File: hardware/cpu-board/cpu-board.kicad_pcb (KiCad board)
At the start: 2 copper layers, 149.4 x 89.9 mm, 39 parts, among them P1 DATA, P2 ADDR1, P3 ADDR2, P4 CTRL1, P5 CTRL2, P6 PWR, P7 IO, SW1 RESET, U1 WD65C02, U2 AT28C256, U3 MXO45HS, U4 74HC132, U5 CY7C199, U6 4012, U7 4012, U8 74HC138, U9 7805

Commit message: layout
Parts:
- moved D1 125.7 mm to (254.0, 57.1)
- moved D2 125.7 mm to (188.0, 54.6)
- moved R6 125.7 mm to (257.8, 57.1)
- moved U9 125.7 mm to (205.7, 55.9)
- moved C12 125.7 mm to (196.8, 55.9)
- moved C7 125.7 mm to (217.2, 55.9)
- moved P6 125.7 mm to (175.3, 59.7)
- moved R7 125.7 mm to (250.2, 57.1)
- moved SW1 125.7 mm to (242.6, 57.1)
- moved C11 125.7 mm to (262.9, 59.7)
- moved C8 125.7 mm to (262.9, 53.3)
- moved R5 125.7 mm to (231.1, 54.6)
- moved C9 83.5 mm to (52.1, 74.9), turned to 180 degrees
- moved U4 62.5 mm to (72.4, 124.5), turned to 270 degrees
- moved P5 55.0 mm to (130.8, 55.9)
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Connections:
- P4 pad 1: +5V -> /VIN
- P4 pad 3: /VIN -> RDY
- P4 pad 4: SYNC -> ~IRQ
- P4 pad 5: ~IRQ -> +5V
- P4 pad 6: RDY -> SYNC
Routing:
- net GND: track 0.00 -> 405.8 mm, vias 0 -> 9
- net PHI2: track 62.5 -> 161.1 mm
- net BE: track 16.5 -> 72.9 mm
- net A14: track 176.0 -> 136.7 mm, vias 6 -> 7
- net A4: track 87.0 -> 125.8 mm, vias 0 -> 4
- net A7: track 87.0 -> 125.1 mm, vias 0 -> 2
- net A8: track 137.3 -> 102.4 mm, vias 6 -> 5
- net A12: track 121.8 -> 87.7 mm
- net Net-(U6-Pad1): track 33.3 -> 0.00 mm
- net /VIN: track 33.3 -> 0.00 mm
- net /~RAMCE: track 39.9 -> 71.6 mm
- net A13: track 121.0 -> 93.5 mm, vias 2 -> 5
- net Net-(R5-Pad1): track 27.1 -> 0.00 mm
- net ~RST: track 45.5 -> 68.6 mm, vias 0 -> 2
- net /Address Decode/~IO6: track 12.7 -> 34.3 mm, vias 0 -> 2
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- removed copper zone on B.Cu, net GND
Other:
- board outline removed

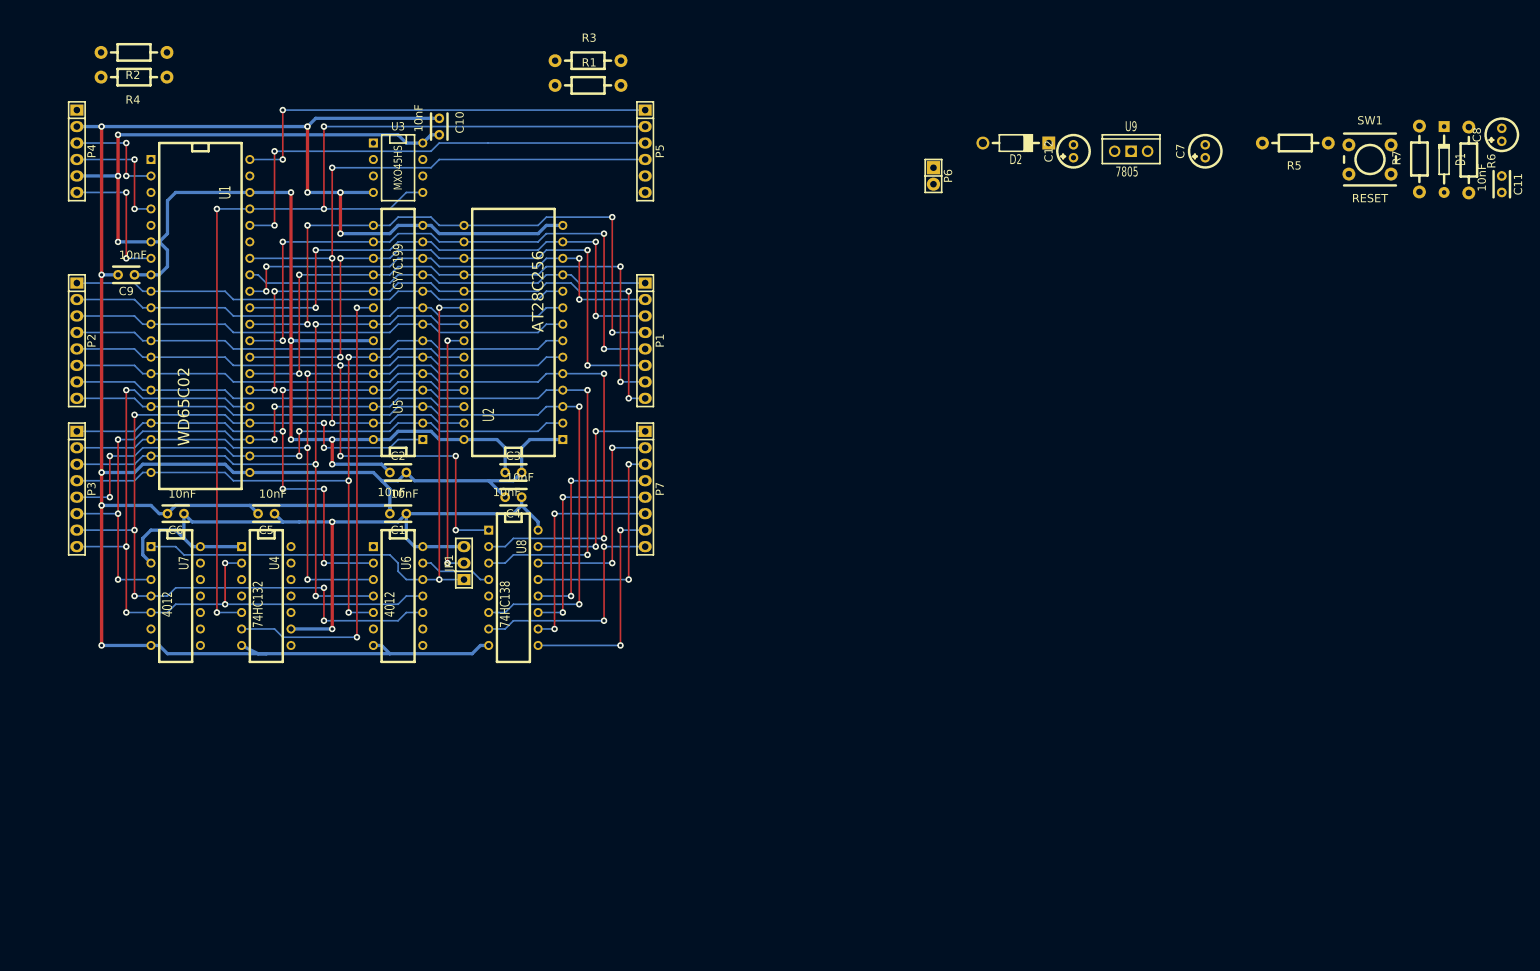
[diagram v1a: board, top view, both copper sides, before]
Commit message: add IO ports to schematic
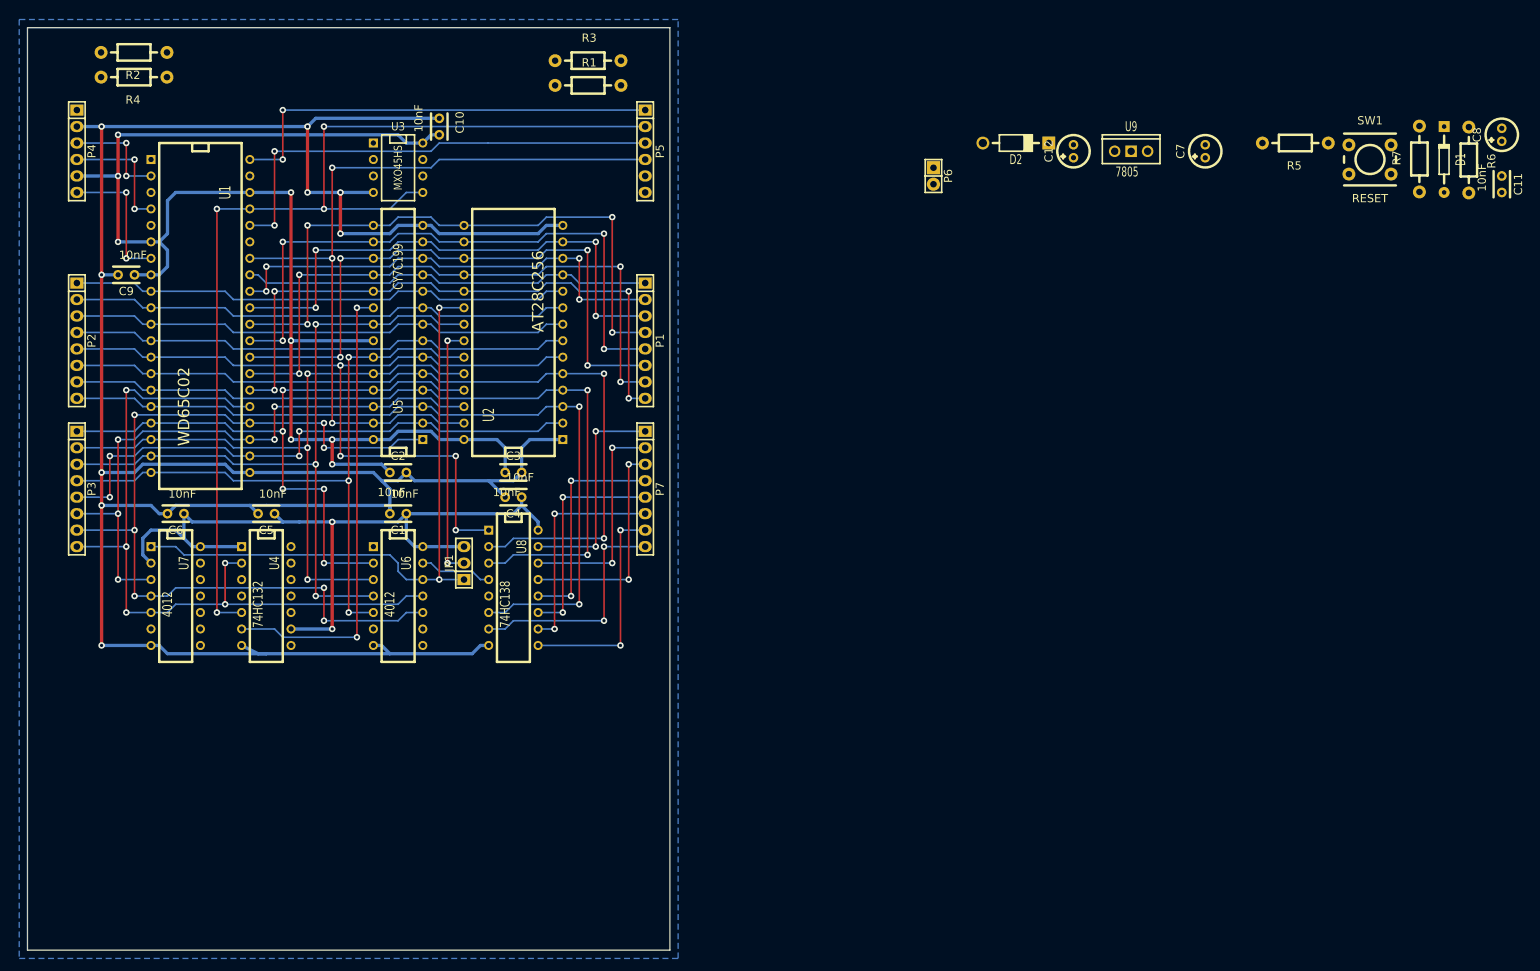
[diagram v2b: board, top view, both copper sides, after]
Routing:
- added copper zone on B.Cu, net GND
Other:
- board outline added: 99.1 x 142.2 mm

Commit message: layout agoun
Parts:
- added C13: 10nF, Capacitors_ThroughHole:Capacitor4x3RM2.5, F.Cu at (130.8, 77.5)
- added CON1: BARREL_JACK, Connect:BARREL_JACK, F.Cu at (43.2, 121.9)
- added JP2: JUMPER3, Pin_Headers:Pin_Header_Straight_1x03, F.Cu at (144.8, 130.8)
- added Outl: EuroBoard160mmX100mm_holes, EuroBoard_Outline:EuroBoard160mmX100mm_holes, F.Cu at (34.3, 135.9)
- added SW2: PWR, IHeartKiCad:SW_M6_PTH, F.Cu at (40.6, 109.2)
- added U10: W65C51N, Sockets_DIP:DIP-28__600_ELL, F.Cu at (124.5, 115.6)
- added X1: CRYSTAL, Crystals:Crystal_HC49-U_Vertical, F.Cu at (147.3, 115.6)
- C6: value 10nF -> 4.7uF
- C7: value 4.7uF -> 10nF
- D1: value 1N4148 -> 1N4001
- D2: value 1N4001 -> 1N4148
- P1: value DATA -> CTRL1; footprint Socket_Strips:Socket_Strip_Straight_1x08 -> Socket_Strips:Socket_Strip_Straight_1x06
- P2: value ADDR1 -> CTRL2; footprint Socket_Strips:Socket_Strip_Straight_1x08 -> Socket_Strips:Socket_Strip_Straight_1x06
- P3: value ADDR2 -> DATA
- P4: value CTRL1 -> IO; footprint Socket_Strips:Socket_Strip_Straight_1x06 -> Socket_Strips:Socket_Strip_Straight_1x08
- P5: value CTRL2 -> ADDR1; footprint Socket_Strips:Socket_Strip_Straight_1x06 -> Socket_Strips:Socket_Strip_Straight_1x08
- P6: value PWR -> ADDR2; footprint Pin_Headers:Pin_Header_Straight_1x02 -> Socket_Strips:Socket_Strip_Straight_1x08
- P7: value IO -> SERIAL; footprint Socket_Strips:Socket_Strip_Straight_1x08 -> Socket_Strips:Socket_Strip_Straight_1x06
- U1: footprint Sockets_DIP:DIP-40__600 -> Sockets_DIP:DIP-40__600_ELL
- U2: footprint Sockets_DIP:DIP-28__600 -> Sockets_DIP:DIP-28__600_ELL
- U3: value MXO45HS -> 74HC132; footprint Sockets_DIP:DIP-8__300 -> Sockets_DIP:DIP-14__300_ELL
- U4: value 74HC132 -> CY7C199; footprint Sockets_DIP:DIP-14__300 -> Sockets_DIP:DIP-28__300_ELL
- U5: value CY7C199 -> MXO45HS; footprint Sockets_DIP:DIP-28__300 -> Sockets_DIP:DIP-8__300_ELL
- U6: value 4012 -> 7805; footprint Sockets_DIP:DIP-14__300 -> Discret:LM78XXV
- U7: footprint Sockets_DIP:DIP-14__300 -> Sockets_DIP:DIP-14__300_ELL
- U8: value 74HC138 -> 4012; footprint Sockets_DIP:DIP-16__300 -> Sockets_DIP:DIP-14__300_ELL
- U9: value 7805 -> 74HC138; footprint Discret:LM78XXV -> Sockets_DIP:DIP-16__300_ELL
- moved D1 218.8 mm to (43.2, 115.6), turned to 0 degrees
- moved C8 217.1 mm to (53.3, 110.2)
- moved C7 175.0 mm to (48.3, 101.6)
- moved C11 160.0 mm to (102.9, 58.4), turned to 90 degrees
- moved R6 104.4 mm to (153.7, 49.5)
- moved P6 102.4 mm to (101.6, 130.8), turned to 0 degrees
- moved R7 94.1 mm to (156.2, 62.2), turned to 0 degrees
- moved P1 92.5 mm to (39.4, 71.1)
- moved P5 91.2 mm to (78.7, 130.8), turned to 0 degrees
- moved U9 88.9 mm to (116.8, 57.1), turned to 0 degrees
- moved JP1 83.6 mm to (179.1, 85.1)
- moved SW1 79.6 mm to (163.8, 45.7)
- moved P4 77.7 mm to (119.4, 40.6), turned to 0 degrees
- moved R5 76.0 mm to (156.2, 67.3)
- moved U7 75.2 mm to (118.1, 78.7), turned to 0 degrees
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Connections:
- C12 pad 1: Net-(C12-Pad1) -> +5V
- C12 pad 2: GND -> Net-(C12-Pad2)
- C8 pad 1: +5V -> Net-(C8-Pad1)
- C8 pad 2: Net-(C8-Pad2) -> GND
- C9 pad 1: +5V -> Net-(C8-Pad1)
- D1 pad 1: GND -> Net-(D1-Pad1)
- D1 pad 2: Net-(C8-Pad2) -> Net-(C8-Pad1)
- D2 pad 1: /VIN -> GND
- D2 pad 2: Net-(C12-Pad1) -> Net-(C12-Pad2)
- P1 pad 1: /D0 -> +5V
- P1 pad 2: /D1 -> GND
- P1 pad 3: /D2 -> RDY
- P1 pad 4: /D3 -> ~IRQ
- P1 pad 5: /D4 -> VIN
- P1 pad 6: /D5 -> SYNC
- P2 pad 1: A0 -> ~RST
- P2 pad 2: A1 -> PHI2
- P2 pad 3: A2 -> BE
- P2 pad 4: A3 -> R/~W
- P2 pad 5: A4 -> (no net)
- P2 pad 6: A5 -> (no net)
- P3 pad 1: A8 -> D0
- P3 pad 2: A9 -> D1
- P3 pad 3: A10 -> D2
- P3 pad 4: A11 -> D3
- P3 pad 5: A12 -> D4
- P3 pad 6: A13 -> D5
- P3 pad 7: A14 -> D6
- P3 pad 8: A15 -> D7
- P4 pad 1: /VIN -> ~IO0
- P4 pad 2: GND -> ~IO1
- P4 pad 3: RDY -> ~IO2
- P4 pad 4: ~IRQ -> ~IO3
- P4 pad 5: +5V -> ~IO4
- P4 pad 6: SYNC -> ~IO5
- P5 pad 1: ~RST -> A0
- P5 pad 2: PHI2 -> A1
- P5 pad 3: BE -> A2
- P5 pad 4: R/~W -> A3
- P5 pad 5: (no net) -> A4
- P5 pad 6: (no net) -> A5
- P6 pad 1: /VIN -> A8
- P6 pad 2: GND -> A9
- P7 pad 1: /Address Decode/~IO0 -> (no net)
- P7 pad 2: /Address Decode/~IO1 -> /IO/TX
- P7 pad 3: /Address Decode/~IO2 -> /IO/RX
- P7 pad 4: /Address Decode/~IO3 -> (no net)
- P7 pad 5: /Address Decode/~IO4 -> /IO/~RTS
- P7 pad 6: /Address Decode/~IO5 -> GND
- R6 pad 1: Net-(C8-Pad2) -> Net-(C12-Pad2)
- R7 pad 2: Net-(C8-Pad2) -> Net-(C12-Pad2)
- U1 pad 26: /D7 -> D7
- U1 pad 27: /D6 -> D6
- U1 pad 28: /D5 -> D5
- U1 pad 29: /D4 -> D4
- U1 pad 30: /D3 -> D3
- U1 pad 31: /D2 -> D2
- U1 pad 32: /D1 -> D1
- U1 pad 33: /D0 -> D0
- U2 pad 11: /D0 -> D0
- U2 pad 12: /D1 -> D1
- U2 pad 13: /D2 -> D2
- U2 pad 15: /D3 -> D3
- U2 pad 16: /D4 -> D4
- U2 pad 17: /D5 -> D5
- U2 pad 18: /D6 -> D6
- U2 pad 19: /D7 -> D7
- U3 pad 1: (no net) -> +5V
- U3 pad 2: (no net) -> A15
- U3 pad 3: (no net) -> Net-(U3-Pad3)
- U3 pad 4: GND -> Net-(U3-Pad3)
- U3 pad 6: (no net) -> /~RAMCE
- U3 pad 7: (no net) -> GND
- U3 pad 8: +5V -> ~RST
- U4 pad 1: +5V -> A14
- U4 pad 10: Net-(R7-Pad1) -> A0
- U4 pad 11: (no net) -> D0
- U4 pad 12: (no net) -> D1
- U4 pad 13: (no net) -> D2
- U4 pad 14: +5V -> GND
- U4 pad 2: A15 -> A12
- U4 pad 3: Net-(U4-Pad3) -> A7
- U4 pad 4: Net-(U4-Pad3) -> A6
- U4 pad 5: PHI2 -> A5
- U4 pad 6: /~RAMCE -> A4
- U4 pad 7: GND -> A3
- U4 pad 8: ~RST -> A2
- U4 pad 9: +5V -> A1
- U5 pad 1: A14 -> (no net)
- U5 pad 2: A12 -> (no net)
- U5 pad 3: A7 -> (no net)
- U5 pad 4: A6 -> GND
- U5 pad 5: A5 -> PHI2
- U5 pad 6: A4 -> (no net)
- U5 pad 7: A3 -> (no net)
- U5 pad 8: A2 -> +5V
- U7 pad 1: /Address Decode/~ROMSEL -> Net-(U7-Pad1)
- U7 pad 10: (no net) -> A14
- U7 pad 11: (no net) -> A15
- U7 pad 12: (no net) -> /Address Decode/~ROMSEL
- U7 pad 13: (no net) -> Net-(U7-Pad13)
- U7 pad 2: +5V -> A8
- U7 pad 3: A13 -> A9
- U7 pad 4: A14 -> A10
- U7 pad 5: A15 -> A11
- U7 pad 9: (no net) -> A12
- U8 pad 1: A4 -> /Address Decode/~ROMSEL
- U8 pad 10: /Address Decode/~IO5 -> +5V
- U8 pad 11: /Address Decode/~IO4 -> A2
- U8 pad 12: /Address Decode/~IO3 -> A3
- U8 pad 13: /Address Decode/~IO2 -> Net-(U3-Pad13)
- U8 pad 14: /Address Decode/~IO1 -> +5V
- U8 pad 2: A5 -> +5V
- U8 pad 3: A6 -> A13
- U8 pad 4: Net-(U6-Pad13) -> A14
- U8 pad 5: Net-(U6-Pad1) -> A15
- U8 pad 6: A7 -> (no net)
- U8 pad 7: /Address Decode/~IO7 -> GND
- U8 pad 8: GND -> (no net)
- U8 pad 9: /Address Decode/~IO6 -> +5V
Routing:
- net ~RST: track 68.6 -> 230.9 mm, vias 2 -> 5
- net D7: track 0.00 -> 97.4 mm, vias 0 -> 2
- net D5: track 0.00 -> 97.4 mm, vias 0 -> 2
- net D6: track 0.00 -> 97.4 mm, vias 0 -> 2
- net D4: track 0.00 -> 97.4 mm, vias 0 -> 2
- net D3: track 0.00 -> 97.4 mm, vias 0 -> 2
- net /Address Decode/~ROMSEL: track 96.8 -> 0.00 mm, vias 2 -> 0
- net /D6: track 95.6 -> 0.00 mm, vias 4 -> 0
- net /D4: track 95.6 -> 0.00 mm, vias 4 -> 0
- net /D5: track 95.6 -> 0.00 mm, vias 4 -> 0
- net /D3: track 95.6 -> 0.00 mm, vias 4 -> 0
- net /D7: track 94.8 -> 0.00 mm, vias 4 -> 0
- net D2: track 0.00 -> 85.4 mm, vias 0 -> 2
- net +5V: track 341.2 -> 426.4 mm, vias 10 -> 22
- net /D2: track 82.9 -> 0.00 mm, vias 4 -> 0
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- removed copper zone on B.Cu, net GND
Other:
- board size 99.1 x 142.2 mm -> 160 x 100 mm
- net class Power: via_dia 1 -> 1.5

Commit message: finish layout
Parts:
- removed C13: 10nF, Capacitors_ThroughHole:Capacitor4x3RM2.5
- removed JP2: JUMPER3, Pin_Headers:Pin_Header_Straight_1x03
- removed P7: SERIAL, Socket_Strips:Socket_Strip_Straight_1x06
- removed U10: W65C51N, Sockets_DIP:DIP-28__600_ELL
- removed X1: CRYSTAL, Crystals:Crystal_HC49-U_Vertical
- added D3: LED, LEDs:LED-5MM, F.Cu at (44.5, 82.5)
- added R8: 330, Resistors_ThroughHole:Resistor_Horizontal_RM10mm, F.Cu at (43.2, 92.7)
- moved JP1 125.9 mm to (53.3, 91.4)
- moved R3 36.9 mm to (95.2, 41.9), turned to 180 degrees
- moved C12 17.8 mm to (156.2, 45.7), turned to 180 degrees
- moved R5 15.3 mm to (162.6, 53.3)
- moved D2 11.5 mm to (137.2, 40.6)
- moved R6 9.25 mm to (151.1, 40.6), turned to 0 degrees
- moved R7 6.35 mm to (160.0, 57.1), turned to 180 degrees
- moved SW1 2.54 mm to (163.8, 43.2)
- moved P5 2.54 mm to (78.7, 133.3)
- moved P6 2.54 mm to (101.6, 133.3)
- moved Outl 1.27 mm to (34.3, 137.2)
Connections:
- U3 pad 11: /IO/ACAISEL -> (no net)
- U3 pad 12: +5V -> (no net)
- U3 pad 13: Net-(U3-Pad13) -> (no net)
- U8 pad 10: +5V -> (no net)
- U8 pad 11: A2 -> (no net)
- U8 pad 12: A3 -> (no net)
- U8 pad 13: Net-(U3-Pad13) -> (no net)
- U8 pad 9: +5V -> (no net)
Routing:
- net /Address Decode/~ROMSEL: track 0.00 -> 95.0 mm, vias 0 -> 5
- net ~RST: track 230.9 -> 147.8 mm, vias 5 -> 3
- net PHI2: track 220.8 -> 159.8 mm, vias 6 -> 4
- net /IO/ACAISEL: track 56.4 -> 0.00 mm
- net /IO/ACAIEN: track 41.9 -> 0.00 mm, vias 2 -> 0
- net Net-(U3-Pad13): track 39.9 -> 0.00 mm, vias 2 -> 0
- net A12: track 108.3 -> 145.9 mm, vias 4 -> 7
- net /IO/XTLI: track 36.9 -> 0.00 mm, vias 1 -> 0
- net Net-(R7-Pad1): track 0.00 -> 36.9 mm, vias 0 -> 2
- net /~ROMOE: track 0.00 -> 29.7 mm, vias 0 -> 2
- net /IO/XTLO: track 29.3 -> 0.00 mm, vias 1 -> 0
- net +5V: track 426.4 -> 454.7 mm, vias 22 -> 17
- net Net-(C12-Pad2): track 0.00 -> 26.6 mm
- net BE: track 38.2 -> 63.8 mm
- net /IO/RX: track 22.9 -> 0.00 mm, vias 2 -> 0
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- added copper zone on B.Cu, net GND

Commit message: first pcb layout
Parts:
- removed the Outl at (34.3, 137.2)
- removed SW2: PWR, IHeartKiCad:SW_M6_PTH
- added C13: 10nF, Capacitors_ThroughHole:Capacitor4x3RM2.5, F.Cu at (153.7, 108.0)
- added Outl: EuroBoard_halb_Type-I_100mmX80mm_holes, EuroBoard_Outline:EuroBoard_halb_Type-I_100mmX80mm_holes, F.Cu at (92.7, 125.7)
- added S1: PWR, switch-misc-PVA2F, F.Cu at (186.7, 110.5)
- moved D3 145.1 mm to (189.2, 91.4)
- moved CON1 143.9 mm to (185.4, 100.3), turned to 180 degrees
- moved R8 142.4 mm to (185.4, 86.4), turned to 0 degrees
- moved D1 142.2 mm to (185.4, 116.8), turned to 180 degrees
- moved C9 129.7 mm to (182.9, 120.7)
- moved C8 125.0 mm to (177.8, 121.9), turned to 270 degrees
- moved U6 119.9 mm to (167.6, 120.7), turned to 270 degrees
- moved C5 112.1 mm to (179.1, 76.2)
- moved C7 111.1 mm to (157.5, 121.9), turned to 270 degrees
- moved C6 110.7 mm to (152.4, 120.7), turned to 270 degrees
- moved JP1 95.8 mm to (148.6, 101.6), turned to 270 degrees
- moved U4 76.5 mm to (127.0, 62.2)
- moved R4 74.0 mm to (105.4, 106.7)
- moved P1 69.1 mm to (97.8, 108.0)
- moved C10 63.1 mm to (153.7, 91.4), turned to 270 degrees
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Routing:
- net GND: track 455.6 -> 318.9 mm, vias 16 -> 0
- net +5V: track 454.7 -> 333.0 mm, vias 17 -> 0
- net A15: track 170.0 -> 90.7 mm, vias 6 -> 0
- net A0: track 70.7 -> 133.3 mm
- net /~RAMCE: track 117.9 -> 56.8 mm, vias 2 -> 0
- net A1: track 70.7 -> 130.5 mm
- net VIN: track 57.5 -> 112.3 mm
- net A9: track 146.4 -> 94.3 mm, vias 8 -> 3
- net A10: track 149.4 -> 104.9 mm, vias 6 -> 2
- net R/~W: track 127.8 -> 172.3 mm, vias 5 -> 0
- net A12: track 145.9 -> 101.6 mm, vias 7 -> 0
- net PHI2: track 159.8 -> 117.4 mm, vias 4 -> 0
- net A14: track 157.4 -> 121.4 mm, vias 8 -> 1
- net A13: track 138.0 -> 103.3 mm, vias 6 -> 2
- net BE: track 63.8 -> 29.9 mm, vias 2 -> 0
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- added copper zone on F.Cu, net GND
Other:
- board size 160 x 100 mm -> 100 x 80 mm
- rule via_min_drill: 0.8 -> 0.5
- rule via_min_size: 1 -> 0.8
- board text added: "+5V"
- board text added: "1"
- board text added: "1,2 NORMAL 2,3 ROM WRITE"
- board text added: "2"
- board text added: "3"
- board text added: "A0"
- board text added: "A1"
- board text added: "A10"
- board text added: "A11"
- board text added: "A12"
- board text added: "A13"
- board text added: "A14"
- board text added: "A15"
- board text added: "A2"
- board text added: "A3"
- board text added: "A4"
- board text added: "A5"
- board text added: "A6"
- board text added: "A7"
- board text added: "A8"
- board text added: "A9"
- board text added: "BE"
- board text added: "BURI microcomputer CPU board"
- board text added: "D0"
- board text added: "D1"
- board text added: "D2"
- board text added: "D3"
- board text added: "D4"
- board text added: "D5"
- board text added: "D6"
- board text added: "D7"
- board text added: "GND"
- board text added: "PHI2"
- board text added: "RDY"
- board text added: "SYNC"
- board text added: "V1.0 (C) 2015 Rich Wareham rich.buri@richwareham.com"
- board text added: "VIN"
- board text added: "https://github.com/rjw57/buri"
- board text added: "~IO0"
- board text added: "~IO1"
- board text added: "~IO2"
- board text added: "~IO3"
- board text added: "~IO4"
- board text added: "~IO5"
- board text added: "~IO6"
- board text added: "~IO7"
- board text added: "~IRQ"
- board text added: "~RST"

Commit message: final version sent to manufacturer
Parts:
- moved S1 22.2 mm to (181.6, 132.1)
- moved C4 22.2 mm to (143.5, 85.1)
- moved C6 22.2 mm to (147.3, 142.2)
- moved JP1 22.2 mm to (143.5, 123.2)
- moved P2 22.2 mm to (92.7, 85.1)
- moved U3 22.2 mm to (161.3, 99.1)
- moved U7 22.2 mm to (161.3, 114.3)
- moved U8 22.2 mm to (161.3, 130.8)
- moved C10 22.2 mm to (148.6, 113.0)
- moved C12 22.2 mm to (160.0, 72.4)
- moved C2 22.2 mm to (100.3, 116.8)
- moved C3 22.2 mm to (148.6, 97.8)
- moved C5 22.2 mm to (174.0, 97.8)
- moved C9 22.2 mm to (177.8, 142.2)
- moved CON1 22.2 mm to (180.3, 121.9)
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
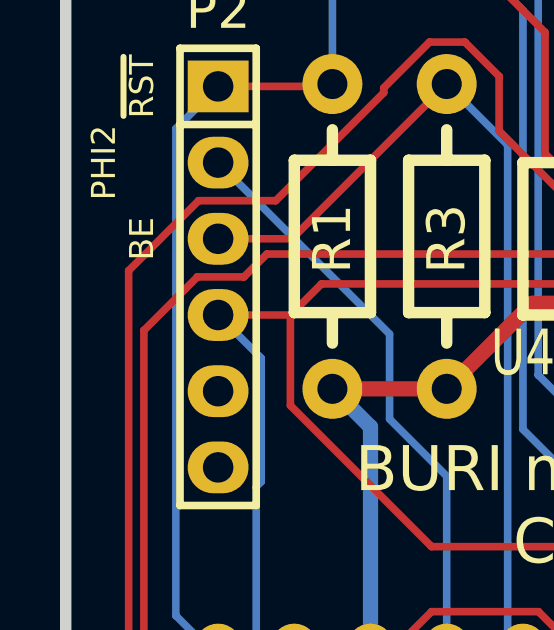
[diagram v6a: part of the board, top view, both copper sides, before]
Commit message: pcb: add label for R/~W connector
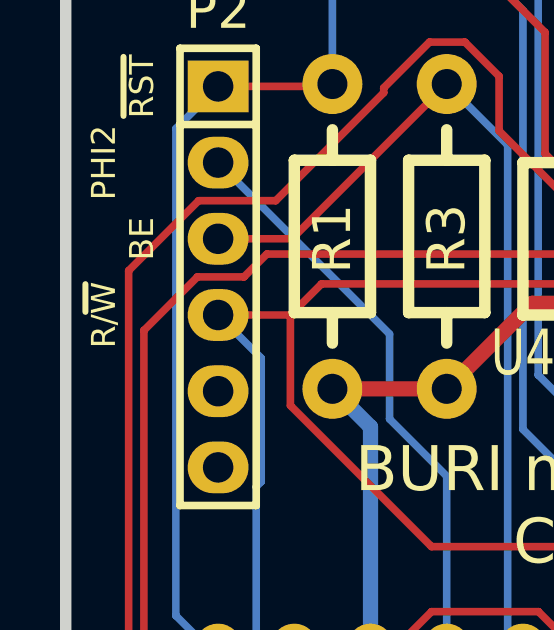
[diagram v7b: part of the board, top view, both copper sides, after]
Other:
- board text added: "R/~W"
